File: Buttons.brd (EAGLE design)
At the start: 85 x 79 mm, 71 parts, among them J1 AVR_SPI_PROG_3X2TESTPOINTS, T1 SI2301, U1 TCA8418RTWR

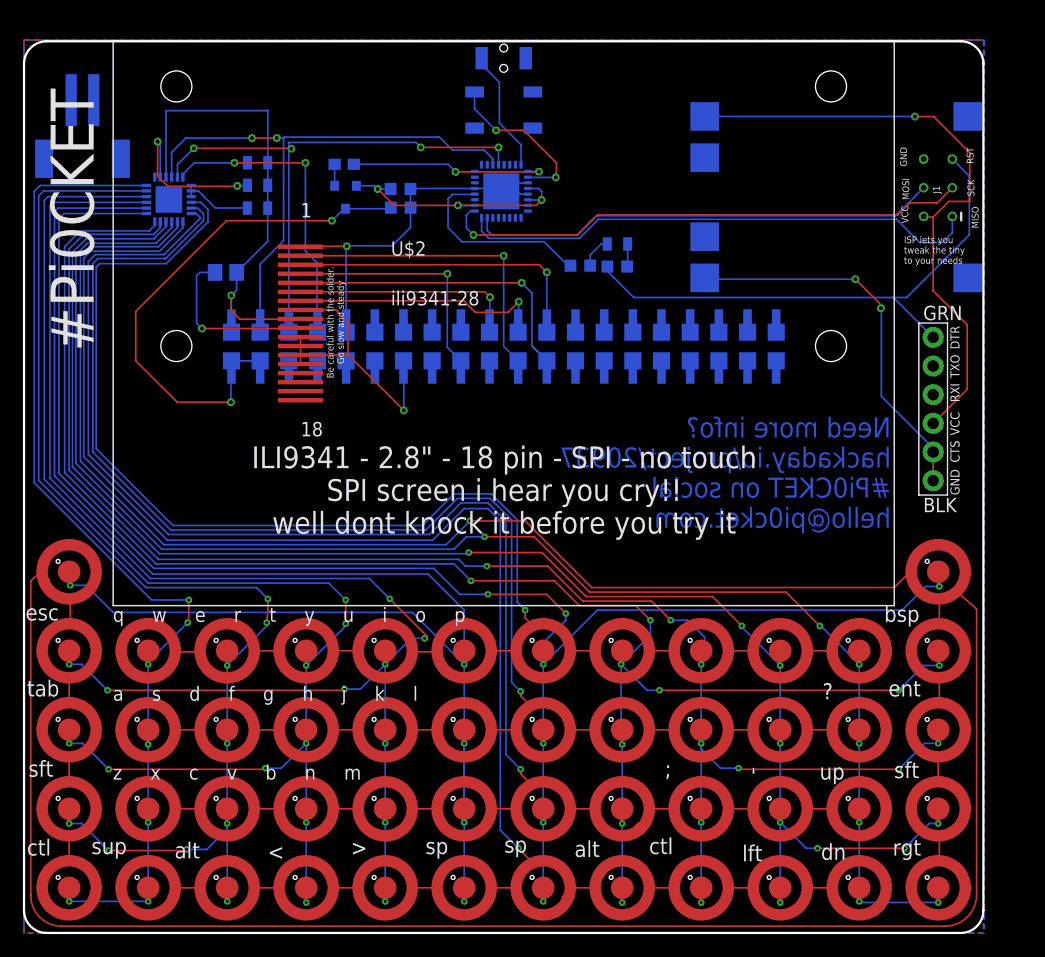
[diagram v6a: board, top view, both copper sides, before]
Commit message: fixed issue with power button footprint
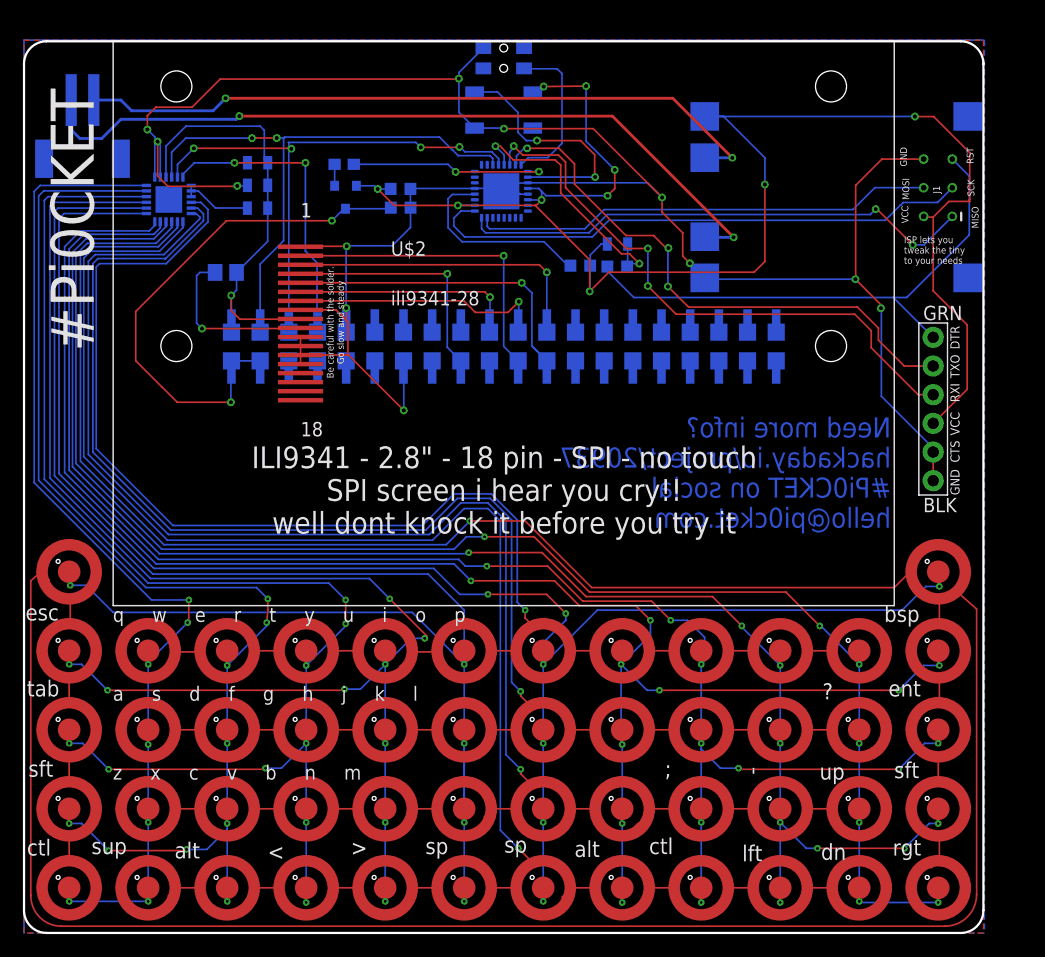
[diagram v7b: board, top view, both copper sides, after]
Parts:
- removed S1: MOMENTARY-SWITCH-SPST-SMD-RIGHT-ANGLE, SparkFun-Switches:TACTILE_SWITCH_SMD_RIGHT_ANGLE
- added S2: EVQ-P7L01P, switch-panasonic:EVQ-P7L01P
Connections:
- net GND: now also S2.B1; no longer S1.2
- net N$1: now also S2.A; no longer S1.1
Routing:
- net GND: track 94.5 -> 194.8 mm, vias 4 -> 10
- net N$37: track 0.00 -> 69.5 mm, vias 0 -> 2
- net VCC: track 80.8 -> 147.3 mm, vias 4 -> 10
- net N$36: track 0.00 -> 62.0 mm, vias 0 -> 2
- net RX: track 0.00 -> 52.2 mm, vias 0 -> 3
- net TX: track 0.00 -> 49.7 mm, vias 0 -> 3
- net N$4: track 2.02 -> 23.6 mm, vias 0 -> 2
- net NEO: track 14.5 -> 21.9 mm
- net 3V3: track 43.8 -> 39.5 mm
- net N$1: track 10.9 -> 14.1 mm
- net ISP-SCK: track 47.1 -> 49.2 mm, vias 1 -> 0
- net ISP-MOSI: track 41.7 -> 41.0 mm
- net SCL: track 49.2 -> 48.7 mm
- net ISP-MISO: track 46.5 -> 46.1 mm, vias 0 -> 2
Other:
- board text added: "This ATmega328 acts as a clever switch"
- board text removed: "This ATtiny88 acts as a clever switch"
